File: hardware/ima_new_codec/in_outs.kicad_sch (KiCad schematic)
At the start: 28 parts, among them J2 InL, J3 InR, J4 OutL, J5 OutR, U2 ${SIM.PARAMS}, U3 ${SIM.PARAMS}, U4 ${SIM.PARAMS}, U5 ${SIM.PARAMS}

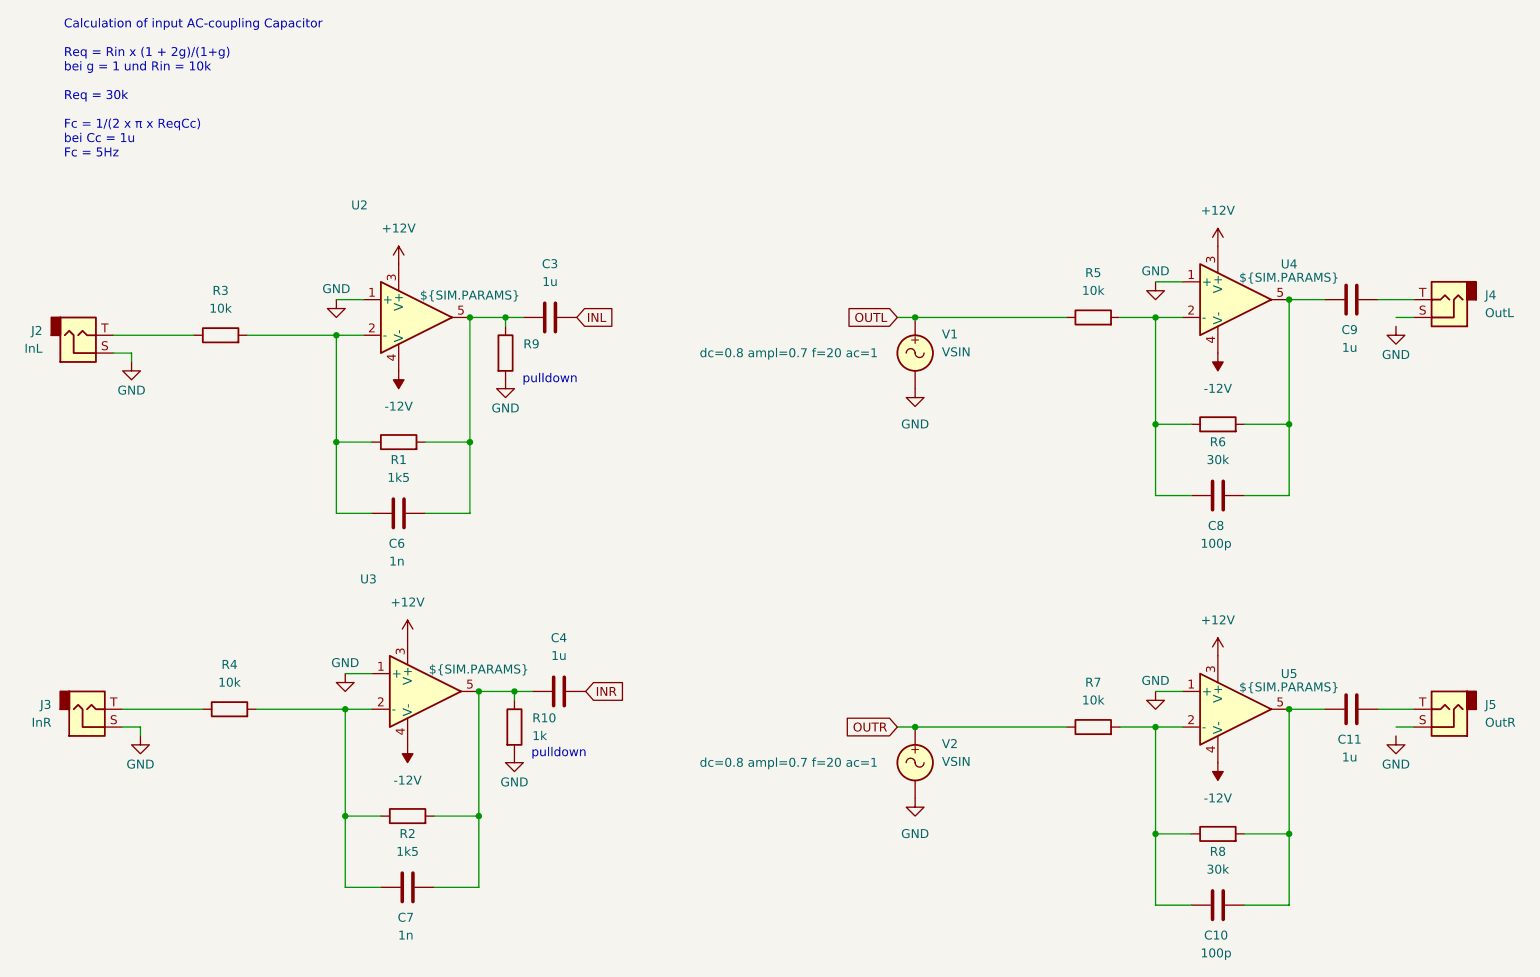
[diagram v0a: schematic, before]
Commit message: changes to in/out stages
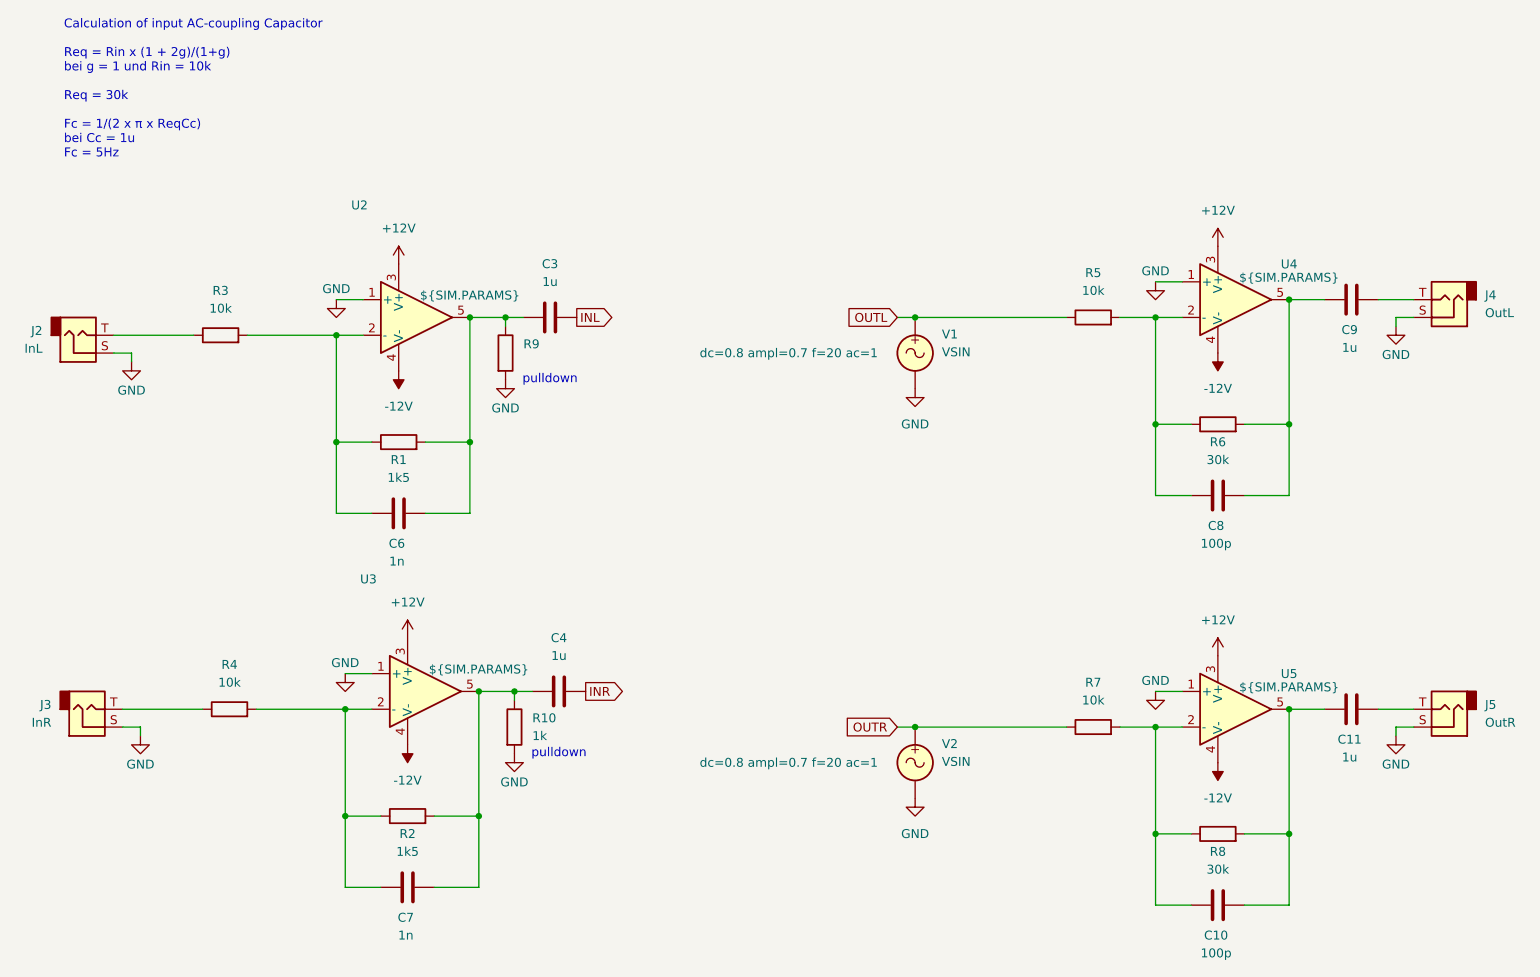
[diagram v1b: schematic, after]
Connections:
- net GND: now also J4.S, J5.S
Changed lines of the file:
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@@
+	(wire
+		(pts
+			(xy 240.03 123.19) (xy 240.03 124.46)
+		)
+		(stroke
+			(width 0)
+			(type default)
+		)
+	)
 	(wire
 		(pts
@@
 		(pts
 			(xy 109.22 118.11) (xy 114.3 118.11)
+		)
+		(stroke
+			(width 0)
+			(type default)
+		)
+	)
+	(wire
+		(pts
+			(xy 240.03 64.77) (xy 240.03 66.04)
 		)
 		(stroke
@@
 	)
 	(global_label "INR"
-		(shape input)
+		(shape output)
 		(at 124.46 118.11 0)
 		(fields_autoplaced yes)
@@
 	)
 	(global_label "INL"
-		(shape input)
+		(shape output)
 		(at 123.19 64.77 0)
 		(fields_autoplaced yes)

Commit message: changes to hardware design
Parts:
- added C14, C15: 10u, symbol Device:C
- added U6: NE5532, symbol Amplifier_Operational:NE5532
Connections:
- net at R4.1: now also C15.2; no longer J3.T
- net at J2.T: now also C14.1; no longer R3.1
- new net: C14.2, R3.1
- new net: C15.1, J3.T
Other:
- note added: "Input Av = 0.15"
- note added: "Output Av = 3.0"
- moved on the sheet: R3
